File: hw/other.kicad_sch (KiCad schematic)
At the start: 41 parts, among them J2 Conn_01x02, U14 NE555P, Y1 Crystal

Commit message: Work on scmenatic and PCB
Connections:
- net ~{NMI}: now also U14.3 (Q)
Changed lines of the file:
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@@
+    (stroke (width 0) (type default))
+  )
+  (wire (pts (xy 210.82 41.91) (xy 208.28 41.91))
     (stroke (width 0) (type default))
   )
@@
     (stroke (width 0) (type default))
   )
+  (wire (pts (xy 210.82 22.86) (xy 210.82 41.91))
+    (stroke (width 0) (type default))
+  )
   (wire (pts (xy 67.31 123.19) (xy 76.2 123.19))
     (stroke (width 0) (type default))
@@
     )
   )
+  (global_label "~{NMI}" (shape input) (at 134.62 120.65 180) (fields_autoplaced)
+    (effects (font (size 1.27 1.27)) (justify right))
+    (property "Intersheetrefs" "${INTERSHEET_REFS}" (at 128.3275 120.65 0)
+      (effects (font (size 1.27 1.27)) (justify right) hide)
+    )
+  )
   (global_label "~{NMI}" (shape input) (at 49.53 86.36 180) (fields_autoplaced)
     (effects (font (size 1.27 1.27)) (justify right))
@@
     )
   )
+  (global_label "~{NMI}" (shape input) (at 210.82 22.86 90) (fields_autoplaced)
+    (effects (font (size 1.27 1.27)) (justify left))
+    (property "Intersheetrefs" "${INTERSHEET_REFS}" (at 210.82 16.5675 90)
+      (effects (font (size 1.27 1.27)) (justify left) hide)
+    )
+  )
+  (global_label "~{RESET}" (shape input) (at 134.62 105.41 180) (fields_autoplaced)
+    (effects (font (size 1.27 1.27)) (justify right))
+    (property "Intersheetrefs" "${INTERSHEET_REFS}" (at 125.9691 105.41 0)
+      (effects (font (size 1.27 1.27)) (justify right) hide)
+    )
+  )
   (global_label "~{RD}" (shape input) (at 49.53 76.2 180) (fields_autoplaced)
     (effects (font (size 1.27 1.27)) (justify right))
@@
       (effects (font (size 1.27 1.27)) (justify right) hide)
     )
+  )
+  (global_label "~{CLK}" (shape input) (at 134.62 113.03 180) (fields_autoplaced)
+    (effects (font (size 1.27 1.27)) (justify right))
+    (property "Intersheetrefs" "${INTERSHEET_REFS}" (at 128.1461 113.03 0)
+      (effects (font (size 1.27 1.27)) (justify right) hide)
+    )

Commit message: Work on scmenatic and PCB
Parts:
- removed C1: C_Polarized, Capacitor_THT:CP_Radial_D5.0mm_P2.50mm, symbol z80mgc:Capacitor
- removed J2: Conn_01x02, Connector_PinHeader_1.00mm:PinHeader_1x02_P1.00mm_Vertical, symbol Connector_Generic:Conn_01x02
- removed U14: NE555P, Package_DIP:DIP-8_W7.62mm, symbol Timer:NE555P
- added C3, C5: 33pF, Capacitor_THT:C_Disc_D4.3mm_W1.9mm_P5.00mm, symbol z80mgc:Capacitor
- added C4: 0.1uf, Capacitor_THT:C_Disc_D3.0mm_W1.6mm_P2.50mm, symbol z80mgc:Capacitor
- added C7, C8, C9 (x2): 0.1uF, Capacitor_THT:C_Disc_D3.0mm_W1.6mm_P2.50mm, symbol z80mgc:Dec_Cap
- added J4: POWER, Connector_PinHeader_1.00mm:PinHeader_1x02_P1.00mm_Vertical, symbol Connector_Generic:Conn_01x02
- added J5: RESET, Connector_PinHeader_1.00mm:PinHeader_1x02_P1.00mm_Vertical, symbol Connector_Generic:Conn_01x02
- added R21: 10k, Resistor_THT:R_Axial_DIN0207_L6.3mm_D2.5mm_P10.16mm_Horizontal, symbol z80mgc:Resistor
- added R22, R23: 1k, Resistor_THT:R_Axial_DIN0207_L6.3mm_D2.5mm_P10.16mm_Horizontal, symbol z80mgc:Resistor
- added U12: NE555P, Package_DIP:DIP-8_W7.62mm, symbol Timer:NE555P
- added U2: 74HC00, Package_DIP:DIP-14_W7.62mm_Socket_LongPads, symbol 74xx:74HC00
- added U3: 74HC04, Package_DIP:DIP-14_W7.62mm_Socket_LongPads, symbol 74xx:74HC04
- added U4: 74HC02, Package_DIP:DIP-14_W7.62mm_Socket_LongPads, symbol 74xx:74HC02
- added U8: 74HC86, Package_DIP:DIP-14_W7.62mm_Socket_LongPads, symbol 74xx:74HC86
- C2: value C_Polarized -> 1uF
- R19: value 10k -> 100k
- R20: value 1k -> 260; footprint Resistor_THT:R_Axial_DIN0207_L6.3mm_D2.5mm_P10.16mm_Horizontal -> Resistor_THT:R_Axial_DIN0204_L3.6mm_D1.6mm_P5.08mm_Horizontal
- Y1: value Crystal -> 6MHz
- renumbered D9 to D10, D10 to D11, D11 to D12, D12 to D13, D13 to D14, D14 to D9, R2 to R10, R3 to R11, R4 to R12, R5 to R13, R6 to R14, R7 to R15, R8 to R16, R9 to R17, R15 to R18, R10 to R2, R11 to R3, R12 to R4, R13 to R5, R14 to R6, R16 to R7, R17 to R8, R18 to R9
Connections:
- net +5V: now also C7.1, C8.1, C9.1, C9.1, J4.1 (Pin_1), R21.2, R23.2, U12.4 (R), U12.8 (VCC), U2.14 (VCC), U3.14 (VCC), U4.14 (VCC), U8.14 (VCC); no longer R19.2
- net GND: now also C3.2, C4.2, C5.2, C7.2, C8.2, C9.2, C9.2, J4.2 (Pin_2), J5.2 (Pin_2), U12.1 (GND), U2.12, U2.13, U2.7 (GND), U3.13, U3.7 (GND), U4.11, U4.12, U4.7 (GND), U8.10, U8.12, U8.13, U8.4, U8.5, U8.7 (GND), U8.9
- net ~{CLK}: now also U3.4
- net ~{NMI}: now also U12.3 (Q)
- net ~{RESET}: now also J5.1 (Pin_1), R23.1
- net at R19.1, R20.2: now also U3.2, U3.3
- net at R20.1: now also Y1.2, C5.1
- net at C2.1: now also R22.1, U12.2 (TR), U12.6 (THR)
- net at Y1.1: now also R19.2, C3.1, U3.1
- new net: R21.1, R22.2, U12.7 (DIS)
- new net: C4.1, U12.5 (CV)
- no-connect marks 2 -> 6
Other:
- moved on the sheet: D1, D10, D11, D12, D13, D14, D15, D16, D17, D2, D3, D4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

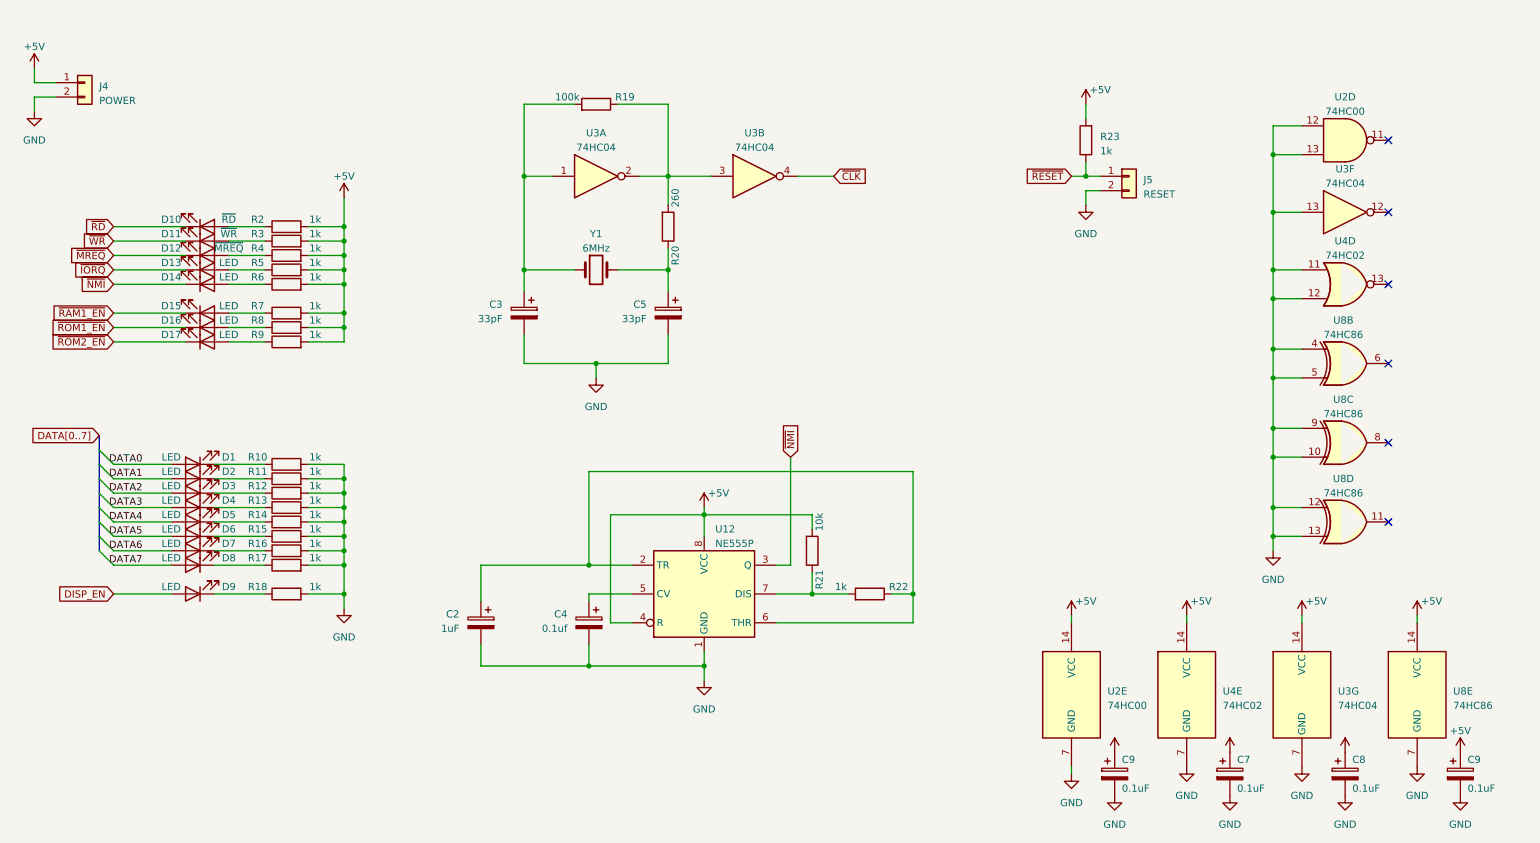
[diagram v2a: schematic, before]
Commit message: Snake working with framebuffer
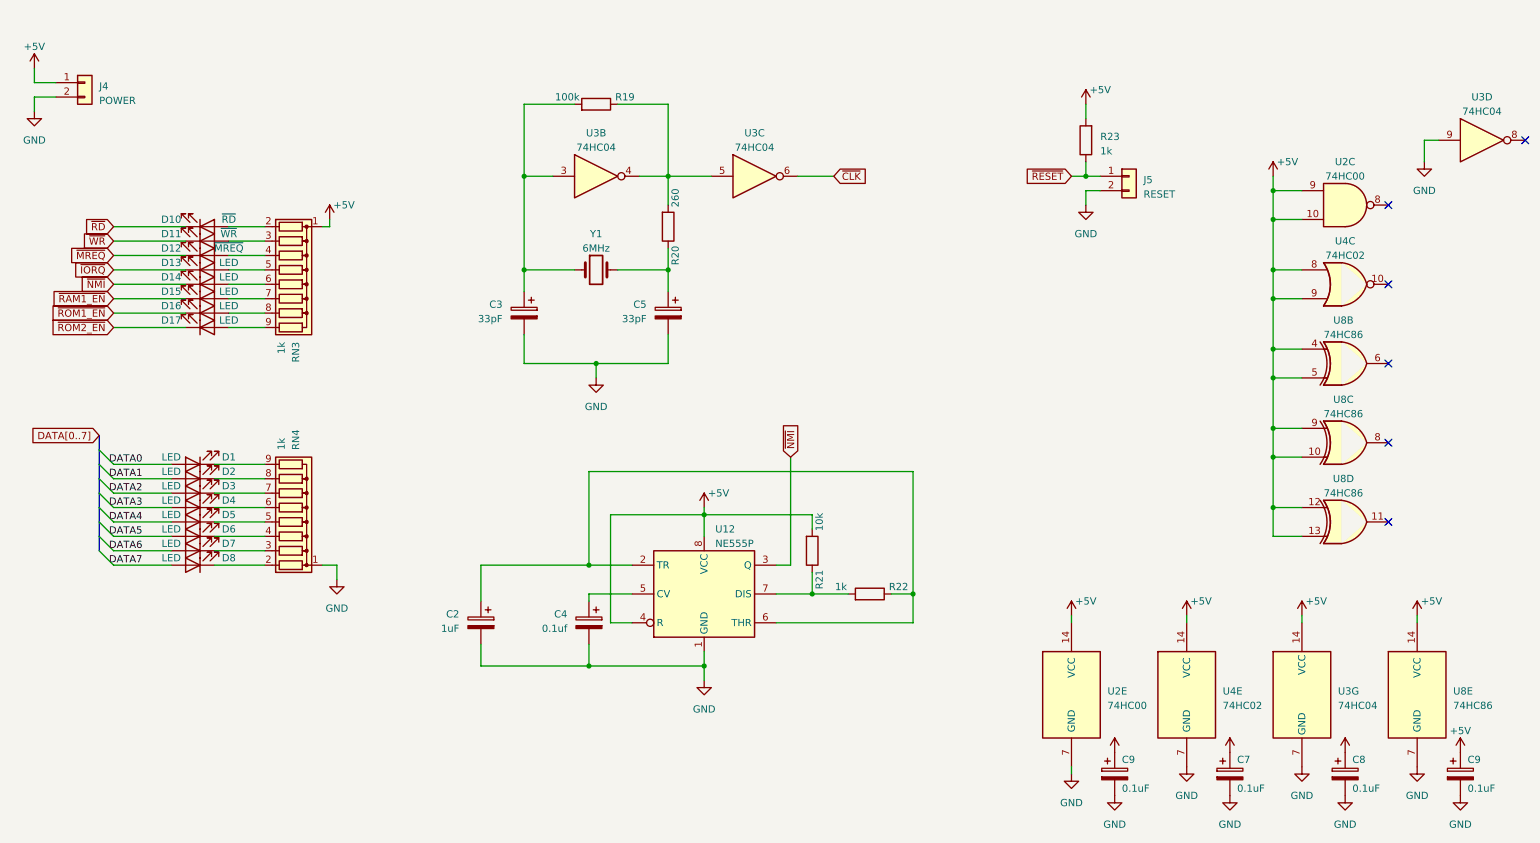
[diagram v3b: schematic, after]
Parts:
- removed D9: LED, LED_THT:LED_D3.0mm, symbol z80mgc:LED_3mm
- removed R10, R11, R12, R13, R14, R15, R16, R17, R18, R2, R3, R4, R5, R6, R7, R8, R9: 1k, Resistor_THT:R_Axial_DIN0207_L6.3mm_D2.5mm_P10.16mm_Horizontal, symbol z80mgc:Resistor
- added RN3, RN4: 1k, Resistor_THT:R_Array_SIP9, symbol Device:R_Network08
- J4: footprint Connector_PinHeader_1.00mm:PinHeader_1x02_P1.00mm_Vertical -> Connector_PinHeader_2.54mm:PinHeader_1x02_P2.54mm_Vertical
- J5: footprint Connector_PinHeader_1.00mm:PinHeader_1x02_P1.00mm_Vertical -> Connector_PinSocket_2.54mm:PinSocket_1x02_P2.54mm_Vertical
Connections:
- net +5V: now also U2.10, U2.9, U4.8, U4.9, U8.10, U8.12, U8.13, U8.4, U8.5, U8.9, RN3.1 (common)
- net GND: now also U3.9, RN4.1 (common); no longer U2.12, U2.13, U3.13, U4.11, U4.12, U8.10, U8.12, U8.13, U8.4, U8.5, U8.9
- net ~{CLK}: now also U3.6; no longer U3.4
- net at D1.1 (K): now also RN4.9 (R8)
- net at D11.2 (A): now also RN3.3 (R2)
- net at D4.1 (K): now also RN4.6 (R5)
- net at D17.2 (A): now also RN3.9 (R8)
- net at D6.1 (K): now also RN4.4 (R3)
- net at D15.2 (A): now also RN3.7 (R6)
- net at D5.1 (K): now also RN4.5 (R4)
- net at D14.2 (A): now also RN3.6 (R5)
- net at D10.2 (A): now also RN3.2 (R1)
- net at D3.1 (K): now also RN4.7 (R6)
- net at D8.1 (K): now also RN4.2 (R1)
- net at D16.2 (A): now also RN3.8 (R7)
- net at R19.1, R20.2: now also U3.4, U3.5; no longer U3.2, U3.3
- net at D12.2 (A): now also RN3.4 (R3)
- net at D13.2 (A): now also RN3.5 (R4)
- net at C3.1, R19.2, Y1.1: now also U3.3; no longer U3.1
- net at D2.1 (K): now also RN4.8 (R7)
- net at D7.1 (K): now also RN4.3 (R2)
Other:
- moved on the sheet: D15, D16, D17, U2C, U3D

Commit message: Fix snake movement bugs
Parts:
- added J2: USB_B, symbol Connector:USB_B
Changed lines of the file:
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@@
+    )
+  )
+  (symbol (lib_id "Connector:USB_B") (at 49.53 25.4 0) (unit 1)
+    (in_bom yes) (on_board yes) (dnp no) (fields_autoplaced)
+    (property "Reference" "J2" (at 49.53 13.97 0)
+      (effects (font (size 1.27 1.27)))
+    )
+    (property "Value" "USB_B" (at 49.53 16.51 0)
+      (effects (font (size 1.27 1.27)))
+    )
+    (property "Footprint" "" (at 53.34 26.67 0)
+      (effects (font (size 1.27 1.27)) hide)
+    )
+    (property "Datasheet" " ~" (at 53.34 26.67 0)
+      (effects (font (size 1.27 1.27)) hide)
+    )
+    (pin "1")
+    (pin "2")
+    (pin "3")
+    (pin "4")
+    (pin "5")
+    (instances
+      (project "z80mgc"
+        (path "/a0755aec-b457-49e5-8300-11792eab574c/0d4dd755-7db3-45ba-b967-0ba9d5a2f689"
+          (reference "J2") (unit 1)
+        )
+      )
     )
   )
